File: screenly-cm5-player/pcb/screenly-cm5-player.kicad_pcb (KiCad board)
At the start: 2 copper layers, 120 x 90 mm, 1 part, among them U1 CM5104064

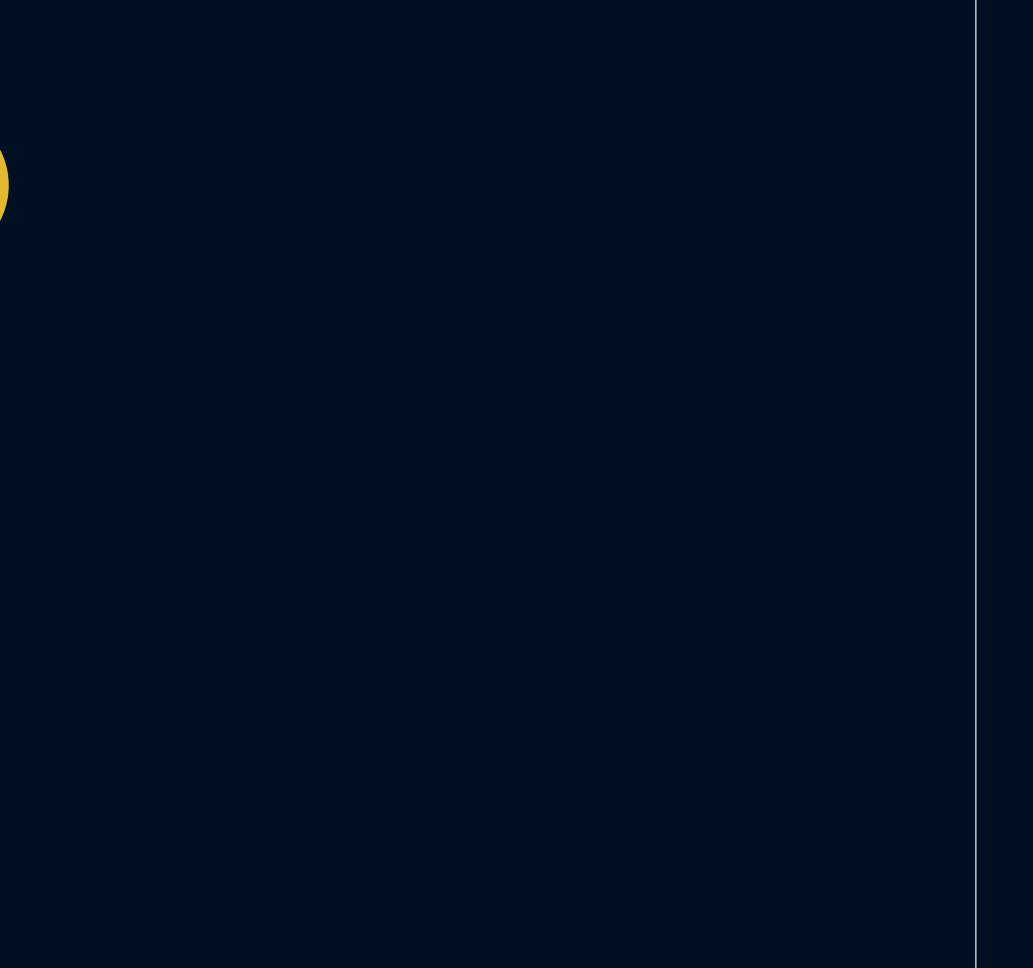
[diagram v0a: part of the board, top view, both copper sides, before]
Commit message: Power stage completed
All power stage has been completed. It has 3 different controlled
outputs USB and PCIe power are separated from the main power due to
safety, durability and cost reasons. PCIe will be DNP later.
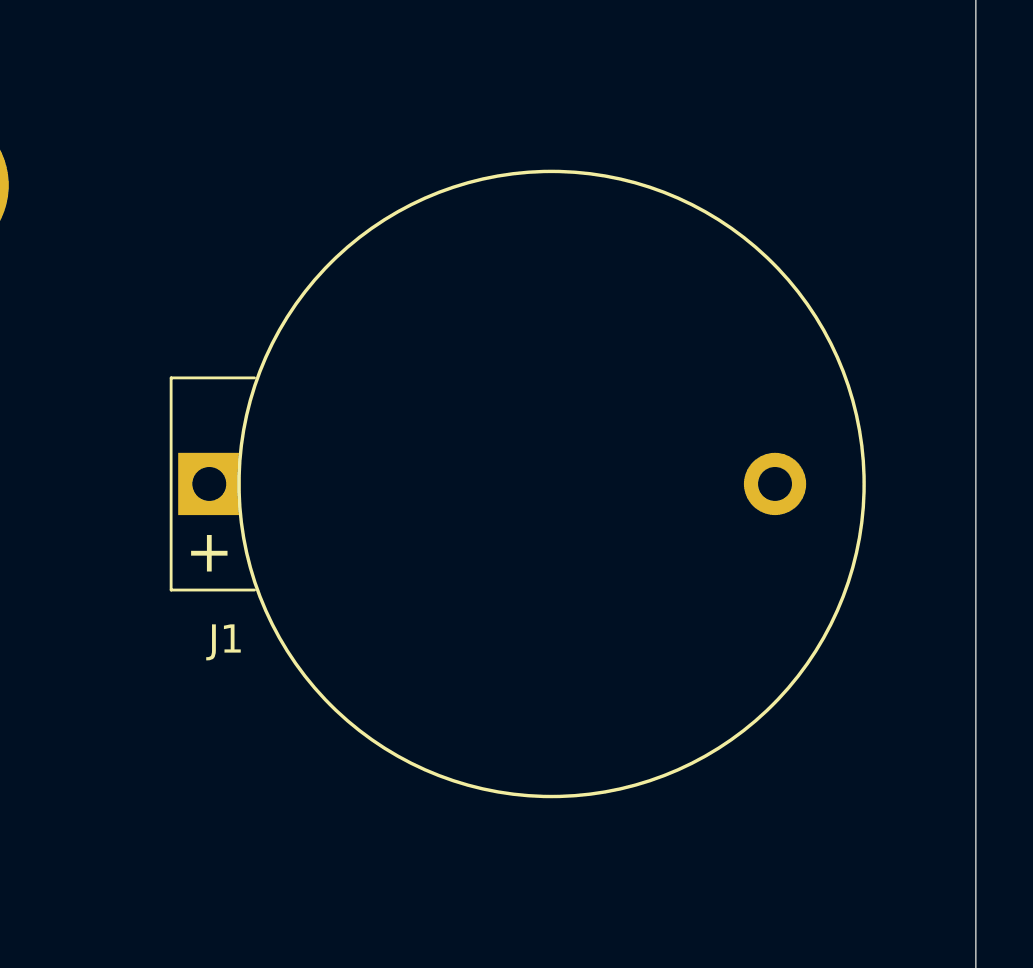
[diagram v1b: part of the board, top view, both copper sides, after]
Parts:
- added J1: CR2032 Holder, Screenly:BatteryHolder_MYOUNG_BS-02_CR2032, F.Cu at (190.0, 80.0)
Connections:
- U1 pad 1: unconnected-(U1A-GND-Pad1) -> GND
- U1 pad 10: unconnected-(U1A-Ethernet_Pair0_N-Pad10) -> /compute_module/ETH.TRD0_N
- U1 pad 100: unconnected-(U1A-CAM_GPIO1-Pad100) -> /compute_module/CAM_GPIO1
- U1 pad 101: unconnected-(U1B-USB_OTG_ID-Pad101) -> /compute_module/USBOTG_ID
- U1 pad 102: unconnected-(U1B-PCIe_nCLKREQ-Pad102) -> /compute_module/PCIE.nCLKREQ
- U1 pad 103: unconnected-(U1B-USB2_N-Pad103) -> /compute_module/USB2.D_N
- U1 pad 104: unconnected-(U1B-PCIE_nWAKE-Pad104) -> /compute_module/PCIE.nWAKE
- U1 pad 105: unconnected-(U1B-USB2_P-Pad105) -> /compute_module/USB2.D_P
- U1 pad 106: unconnected-(U1B-PCIE_PWR_EN-Pad106) -> /compute_module/PCIE.PWR_EN
- U1 pad 107: unconnected-(U1B-GND-Pad107) -> GND
- U1 pad 108: unconnected-(U1B-GND-Pad108) -> GND
- U1 pad 109: unconnected-(U1B-PCIe_nRST-Pad109) -> /compute_module/PCIE.nRST
- U1 pad 11: unconnected-(U1A-Ethernet_Pair2_P-Pad11) -> /compute_module/ETH.TRD2_P
- U1 pad 110: unconnected-(U1B-PCIe_CLK_P-Pad110) -> /compute_module/PCIE.CLK_P
- U1 pad 111: unconnected-(U1B-VBUS_EN-Pad111) -> /compute_module/VBUS_EN
- U1 pad 112: unconnected-(U1B-PCIe_CLK_N-Pad112) -> /compute_module/PCIE.CLK_N
- U1 pad 113: unconnected-(U1B-GND-Pad113) -> GND
- U1 pad 114: unconnected-(U1B-GND-Pad114) -> GND
- U1 pad 115: unconnected-(U1B-MIPI0_D0_N-Pad115) -> /compute_module/DPHY0_P.D0_N
- U1 pad 116: unconnected-(U1B-PCIe_RX_P-Pad116) -> /compute_module/PCIE.RX_P
- U1 pad 117: unconnected-(U1B-MIPI0_D0_P-Pad117) -> /compute_module/DPHY0_P.D0_P
- U1 pad 118: unconnected-(U1B-PCIe_RX_N-Pad118) -> /compute_module/PCIE.RX_N
- U1 pad 119: unconnected-(U1B-GND-Pad119) -> GND
- U1 pad 12: unconnected-(U1A-Ethernet_Pair0_P-Pad12) -> /compute_module/ETH.TRD0_P
- U1 pad 120: unconnected-(U1B-GND-Pad120) -> GND
- U1 pad 121: unconnected-(U1B-MIPI0_D1_N-Pad121) -> /compute_module/DPHY0_P.D1_N
- U1 pad 122: unconnected-(U1B-PCIe_TX_P-Pad122) -> /compute_module/PCIE.TX_P
- U1 pad 123: unconnected-(U1B-MIPI0_D1_P-Pad123) -> /compute_module/DPHY0_P.D1_P
- U1 pad 124: unconnected-(U1B-PCIe_TX_N-Pad124) -> /compute_module/PCIE.TX_N
- U1 pad 125: unconnected-(U1B-GND-Pad125) -> GND
- U1 pad 126: unconnected-(U1B-GND-Pad126) -> GND
- U1 pad 127: unconnected-(U1B-MIPI0_C_N-Pad127) -> /compute_module/DPHY0_P.C_N
- U1 pad 128: unconnected-(U1B-USB3-0-RX_N-Pad128) -> /compute_module/USB3_0.RX_N
- U1 pad 129: unconnected-(U1B-MIPI0_C_P-Pad129) -> /compute_module/DPHY0_P.C_P
- U1 pad 13: unconnected-(U1A-GND-Pad13) -> GND
- U1 pad 130: unconnected-(U1B-USB3-0-RX_P-Pad130) -> /compute_module/USB3_0.RX_P
- U1 pad 131: unconnected-(U1B-GND-Pad131) -> GND
- U1 pad 132: unconnected-(U1B-GND-Pad132) -> GND
- U1 pad 133: unconnected-(U1B-MIPI0_D2_N-Pad133) -> /compute_module/DPHY0_P.D2_N
- U1 pad 134: unconnected-(U1B-USB3-0-D_P-Pad134) -> /compute_module/USB3_0.D_P
- U1 pad 135: unconnected-(U1B-MIPI0_D2_P-Pad135) -> /compute_module/DPHY0_P.D2_P
- U1 pad 136: unconnected-(U1B-USB3-0-D_N-Pad136) -> /compute_module/USB3_0.D_N
- U1 pad 137: unconnected-(U1B-GND-Pad137) -> GND
- U1 pad 138: unconnected-(U1B-GND-Pad138) -> GND
- U1 pad 139: unconnected-(U1B-MIPI0_D3_N-Pad139) -> /compute_module/DPHY0_P.D3_N
- U1 pad 14: unconnected-(U1A-GND-Pad14) -> GND
- U1 pad 140: unconnected-(U1B-USB3-0-TX_N-Pad140) -> /compute_module/USB3_0.TX_N
- U1 pad 141: unconnected-(U1B-MIPI0_D3_P-Pad141) -> /compute_module/DPHY0_P.D3_P
- U1 pad 142: unconnected-(U1B-USB3-0-TX_P-Pad142) -> /compute_module/USB3_0.TX_P
- U1 pad 143: unconnected-(U1B-HDMI1_HOTPLUG-Pad143) -> /compute_module/HDMI1.HOTPLUG
- U1 pad 144: unconnected-(U1B-GND-Pad144) -> GND
- U1 pad 145: unconnected-(U1B-HDMI1_SDA-Pad145) -> /compute_module/HDMI1.SDA
- U1 pad 146: unconnected-(U1B-HDMI1_TX2_P-Pad146) -> /compute_module/HDMI1.D2_P
- U1 pad 147: unconnected-(U1B-HDMI1_SCL-Pad147) -> /compute_module/HDMI1.SCL
- U1 pad 148: unconnected-(U1B-HDMI1_TX2_N-Pad148) -> /compute_module/HDMI1.D2_N
- U1 pad 149: unconnected-(U1B-HDMI1_CEC-Pad149) -> /compute_module/HDMI1.CEC
- U1 pad 15: unconnected-(U1A-Ethernet_nLED3(3.3v)-Pad15) -> /compute_module/ETH_nLED_ACTIVITY
- U1 pad 150: unconnected-(U1B-GND-Pad150) -> GND
- U1 pad 151: unconnected-(U1B-HDMI0_CEC-Pad151) -> /compute_module/HDMI0.CEC
- U1 pad 152: unconnected-(U1B-HDMI1_TX1_P-Pad152) -> /compute_module/HDMI1.D1_P
- U1 pad 153: unconnected-(U1B-HDMI0_HOTPLUG-Pad153) -> /compute_module/HDMI0.HOTPLUG
- U1 pad 154: unconnected-(U1B-HDMI1_TX1_N-Pad154) -> /compute_module/HDMI1.D1_N
- U1 pad 155: unconnected-(U1B-GND-Pad155) -> GND
- U1 pad 156: unconnected-(U1B-GND-Pad156) -> GND
- U1 pad 157: unconnected-(U1B-USB3-1-RX_N-Pad157) -> /compute_module/USB3_1.RX_N
- U1 pad 158: unconnected-(U1B-HDMI1_TX0_P-Pad158) -> /compute_module/HDMI1.D0_P
- U1 pad 159: unconnected-(U1B-USB3-1-RX_P-Pad159) -> /compute_module/USB3_1.RX_P
- U1 pad 16: unconnected-(U1A-FAN_TACHO-Pad16) -> /compute_module/FAN_TACHO
- U1 pad 160: unconnected-(U1B-HDMI1_TX0_N-Pad160) -> /compute_module/HDMI1.D0_N
- U1 pad 161: unconnected-(U1B-GND-Pad161) -> GND
- U1 pad 162: unconnected-(U1B-GND-Pad162) -> GND
- U1 pad 163: unconnected-(U1B-USB3-1-D_P-Pad163) -> /compute_module/USB3_1.D_P
- U1 pad 164: unconnected-(U1B-HDMI1_CLK_P-Pad164) -> /compute_module/HDMI1.CK_P
- U1 pad 165: unconnected-(U1B-USB3-1-D_N-Pad165) -> /compute_module/USB3_1.D_N
- U1 pad 166: unconnected-(U1B-HDMI1_CLK_N-Pad166) -> /compute_module/HDMI1.CK_N
- U1 pad 167: unconnected-(U1B-GND-Pad167) -> GND
- U1 pad 168: unconnected-(U1B-GND-Pad168) -> GND
- U1 pad 169: unconnected-(U1B-USB3-1-TX_N-Pad169) -> /compute_module/USB3_1.TX_N
- U1 pad 17: unconnected-(U1A-Ethernet_nLED2(3.3v)-Pad17) -> /compute_module/nLED_SPEED_100_1000
- U1 pad 170: unconnected-(U1B-HDMI0_TX2_P-Pad170) -> /compute_module/HDMI0.D2_P
- U1 pad 171: unconnected-(U1B-USB3-1-TX_P-Pad171) -> /compute_module/USB3_1.TX_P
- U1 pad 172: unconnected-(U1B-HDMI0_TX2_N-Pad172) -> /compute_module/HDMI0.D2_N
- U1 pad 173: unconnected-(U1B-GND-Pad173) -> GND
- U1 pad 174: unconnected-(U1B-GND-Pad174) -> GND
- U1 pad 175: unconnected-(U1B-MIPI1_D0_N-Pad175) -> /compute_module/DPHY1_P.D0_N
- U1 pad 176: unconnected-(U1B-HDMI0_TX1_P-Pad176) -> /compute_module/HDMI0.D1_P
- U1 pad 177: unconnected-(U1B-MIPI1_D0_P-Pad177) -> /compute_module/DPHY1_P.D0_P
- U1 pad 178: unconnected-(U1B-HDMI0_TX1_N-Pad178) -> /compute_module/HDMI0.D1_N
- U1 pad 179: unconnected-(U1B-GND-Pad179) -> GND
- U1 pad 18: unconnected-(U1A-Ethernet_SYNC_OUT(3.3v)-Pad18) -> /compute_module/SYNC_OUT
- U1 pad 180: unconnected-(U1B-GND-Pad180) -> GND
- U1 pad 181: unconnected-(U1B-MIPI1_D1_N-Pad181) -> /compute_module/DPHY1_P.D1_N
- U1 pad 182: unconnected-(U1B-HDMI0_TX0_P-Pad182) -> /compute_module/HDMI0.D0_P
- U1 pad 183: unconnected-(U1B-MIPI1_D1_P-Pad183) -> /compute_module/DPHY1_P.D1_P
- U1 pad 184: unconnected-(U1B-HDMI0_TX0_N-Pad184) -> /compute_module/HDMI0.D0_N
- U1 pad 185: unconnected-(U1B-GND-Pad185) -> GND
- U1 pad 186: unconnected-(U1B-GND-Pad186) -> GND
- U1 pad 187: unconnected-(U1B-MIPI1_C_N-Pad187) -> /compute_module/DPHY1_P.C_N
- U1 pad 188: unconnected-(U1B-HDMI0_CLK_P-Pad188) -> /compute_module/HDMI0.CK_P
- U1 pad 189: unconnected-(U1B-MIPI1_C_P-Pad189) -> /compute_module/DPHY1_P.C_P
- U1 pad 19: unconnected-(U1A-FAN_PWM-Pad19) -> /compute_module/FAN_PWM
- U1 pad 190: unconnected-(U1B-HDMI0_CLK_N-Pad190) -> /compute_module/HDMI0.CK_N
- U1 pad 191: unconnected-(U1B-GND-Pad191) -> GND
- U1 pad 192: unconnected-(U1B-GND-Pad192) -> GND
- U1 pad 193: unconnected-(U1B-MIPI1_D2_N-Pad193) -> /compute_module/DPHY1_P.D2_N
- U1 pad 194: unconnected-(U1B-MIPI1_D3_N-Pad194) -> /compute_module/DPHY1_P.D3_N
- U1 pad 195: unconnected-(U1B-MIPI1_D2_P-Pad195) -> /compute_module/DPHY1_P.D2_P
- U1 pad 196: unconnected-(U1B-MIPI1_D3_P-Pad196) -> /compute_module/DPHY1_P.D3_P
- U1 pad 197: unconnected-(U1B-GND-Pad197) -> GND
- U1 pad 198: unconnected-(U1B-GND-Pad198) -> GND
- U1 pad 199: unconnected-(U1B-HDMI0_SDA-Pad199) -> /compute_module/HDMI0.SDA
- U1 pad 2: unconnected-(U1A-GND-Pad2) -> GND
- U1 pad 20: unconnected-(U1A-EEPROM_nWP-Pad20) -> /compute_module/EEPROM_nWP
- U1 pad 200: unconnected-(U1B-HDMI0_SCL-Pad200) -> /compute_module/HDMI0.SCL
- U1 pad 21: unconnected-(U1A-LED_nACT-Pad21) -> /compute_module/nLED_ACTIVITY
- U1 pad 22: unconnected-(U1A-GND-Pad22) -> GND
- U1 pad 23: unconnected-(U1A-GND-Pad23) -> GND
- U1 pad 24: unconnected-(U1A-GPIO26-Pad24) -> /compute_module/GPIO26
- U1 pad 25: unconnected-(U1A-GPIO21-Pad25) -> /compute_module/SCLK_GPIO21
- U1 pad 26: unconnected-(U1A-GPIO19-Pad26) -> /compute_module/MISO_GPIO19
- U1 pad 27: unconnected-(U1A-GPIO20-Pad27) -> /compute_module/MOSI_GPIO20
- U1 pad 28: unconnected-(U1A-GPIO13-Pad28) -> /compute_module/GPIO13
- U1 pad 29: unconnected-(U1A-GPIO16-Pad29) -> /compute_module/GPIO16
- U1 pad 3: unconnected-(U1A-Ethernet_Pair3_P-Pad3) -> /compute_module/ETH.TRD3_P
- U1 pad 30: unconnected-(U1A-GPIO6-Pad30) -> /compute_module/GPIO6
- U1 pad 31: unconnected-(U1A-GPIO12-Pad31) -> /compute_module/GPIO12
- U1 pad 32: unconnected-(U1A-GND-Pad32) -> GND
- U1 pad 33: unconnected-(U1A-GND-Pad33) -> GND
- U1 pad 34: unconnected-(U1A-GPIO5-Pad34) -> /compute_module/GPIO5
- U1 pad 35: unconnected-(U1A-ID_SC-Pad35) -> /compute_module/ID_SC
- U1 pad 36: unconnected-(U1A-ID_SD-Pad36) -> /compute_module/ID_SD
- U1 pad 37: unconnected-(U1A-GPIO7-Pad37) -> /compute_module/GPIO7
- U1 pad 38: unconnected-(U1A-GPIO11-Pad38) -> /compute_module/GPIO11
- U1 pad 39: unconnected-(U1A-GPIO8-Pad39) -> /compute_module/GPIO8
- U1 pad 4: unconnected-(U1A-Ethernet_Pair1_P-Pad4) -> /compute_module/ETH.TRD1_P
- U1 pad 40: unconnected-(U1A-GPIO9-Pad40) -> /compute_module/GPIO9
- U1 pad 41: unconnected-(U1A-GPIO25-Pad41) -> /compute_module/DC_GPI25
- U1 pad 42: unconnected-(U1A-GND-Pad42) -> GND
- U1 pad 43: unconnected-(U1A-GND-Pad43) -> GND
- U1 pad 44: unconnected-(U1A-GPIO10-Pad44) -> /compute_module/GPIO10
- U1 pad 45: unconnected-(U1A-GPIO24-Pad45) -> /compute_module/BL_GPIO24
- U1 pad 46: unconnected-(U1A-GPIO22-Pad46) -> /compute_module/GPIO22
- U1 pad 47: unconnected-(U1A-GPIO23-Pad47) -> /compute_module/GPIO23
- U1 pad 48: unconnected-(U1A-GPIO27-Pad48) -> /compute_module/RST_GPIO27
- U1 pad 49: unconnected-(U1A-GPIO18-Pad49) -> /compute_module/CS_GPIO18
- U1 pad 5: unconnected-(U1A-Ethernet_Pair3_N-Pad5) -> /compute_module/ETH.TRD3_N
- U1 pad 50: unconnected-(U1A-GPIO17-Pad50) -> /compute_module/GPIO17
- U1 pad 51: unconnected-(U1A-GPIO15-Pad51) -> /compute_module/GPIO15
- U1 pad 52: unconnected-(U1A-GND-Pad52) -> GND
- U1 pad 53: unconnected-(U1A-GND-Pad53) -> GND
- U1 pad 54: unconnected-(U1A-GPIO4-Pad54) -> /compute_module/GPIO4
- U1 pad 55: unconnected-(U1A-GPIO14-Pad55) -> /compute_module/GPIO14
- U1 pad 56: unconnected-(U1A-GPIO3-Pad56) -> /compute_module/SCL1_IO3
- U1 pad 57: unconnected-(U1A-SD_CLK-Pad57) -> /compute_module/SD_CLK
- U1 pad 58: unconnected-(U1A-GPIO2-Pad58) -> /compute_module/SDA1_IO2
- U1 pad 59: unconnected-(U1A-GND-Pad59) -> GND
- U1 pad 6: unconnected-(U1A-Ethernet_Pair1_N-Pad6) -> /compute_module/ETH.TRD1_N
- U1 pad 60: unconnected-(U1A-GND-Pad60) -> GND
- U1 pad 61: unconnected-(U1A-SD_DAT3-Pad61) -> /compute_module/SD_DAT3
- U1 pad 62: unconnected-(U1A-SD_CMD-Pad62) -> /compute_module/SD_CMD
- U1 pad 63: unconnected-(U1A-SD_DAT0-Pad63) -> /compute_module/SD_DAT0
- U1 pad 65: unconnected-(U1A-GND-Pad65) -> GND
- U1 pad 66: unconnected-(U1A-GND-Pad66) -> GND
- U1 pad 67: unconnected-(U1A-SD_DAT1-Pad67) -> /compute_module/SD_DAT1
- U1 pad 69: unconnected-(U1A-SD_DAT2-Pad69) -> /compute_module/SD_DAT2
- U1 pad 7: unconnected-(U1A-GND-Pad7) -> GND
- U1 pad 71: unconnected-(U1A-GND-Pad71) -> GND
- U1 pad 74: unconnected-(U1A-GND-Pad74) -> GND
- U1 pad 75: unconnected-(U1A-SD_PWR_ON-Pad75) -> /compute_module/SD_PWR_ON
- U1 pad 76: unconnected-(U1A-VBAT-Pad76) -> +BATT
- U1 pad 77: unconnected-(U1A-+5v_(Input)-Pad77) -> /compute_module/+5V
- U1 pad 78: unconnected-(U1A-GPIO_VREF(1.8v/3.3v_Input)-Pad78) -> /compute_module/GPIO_VREF
- U1 pad 79: unconnected-(U1A-+5v_(Input)-Pad79) -> /compute_module/+5V
- U1 pad 8: unconnected-(U1A-GND-Pad8) -> GND
- U1 pad 80: unconnected-(U1A-SCL0-Pad80) -> /compute_module/SCL0
- U1 pad 81: unconnected-(U1A-+5v_(Input)-Pad81) -> /compute_module/+5V
- U1 pad 82: unconnected-(U1A-SDA0-Pad82) -> /compute_module/SDA0
- U1 pad 83: unconnected-(U1A-+5v_(Input)-Pad83) -> /compute_module/+5V
- U1 pad 84: unconnected-(U1A-+3.3v_(Output)-Pad84) -> /compute_module/3V3_CM4
- U1 pad 85: unconnected-(U1A-+5v_(Input)-Pad85) -> /compute_module/+5V
- U1 pad 86: unconnected-(U1A-+3.3v_(Output)-Pad86) -> /compute_module/3V3_CM4
- U1 pad 87: unconnected-(U1A-+5v_(Input)-Pad87) -> /compute_module/+5V
- U1 pad 88: unconnected-(U1A-+1.8v_(Output)-Pad88) -> /compute_module/1V8_CM4
- U1 pad 89: unconnected-(U1A-WiFi_nDisable-Pad89) -> /compute_module/WL_nDis
- U1 pad 9: unconnected-(U1A-Ethernet_Pair2_N-Pad9) -> /compute_module/ETH.TRD2_N
- U1 pad 90: unconnected-(U1A-+1.8v_(Output)-Pad90) -> /compute_module/1V8_CM4
- U1 pad 91: unconnected-(U1A-BT_nDisable-Pad91) -> /compute_module/BT_nDis
- U1 pad 92: unconnected-(U1A-PWR_BUT-Pad92) -> /compute_module/PWR_BUT
- U1 pad 93: unconnected-(U1A-nRPIBOOT-Pad93) -> /compute_module/nRPIBOOT
- U1 pad 94: unconnected-(U1A-CC1-Pad94) -> /compute_module/CC1
- U1 pad 95: unconnected-(U1A-LED_nPWR-Pad95) -> /compute_module/PI_nLED_PWR
- U1 pad 96: unconnected-(U1A-CC2-Pad96) -> /compute_module/CC2
- U1 pad 97: unconnected-(U1A-CAM_GPIO0-Pad97) -> /compute_module/CAM_GPIO0
- U1 pad 98: unconnected-(U1A-GND-Pad98) -> GND
- U1 pad 99: unconnected-(U1A-PMIC_ENABLE-Pad99) -> /compute_module/GLOBAL_EN

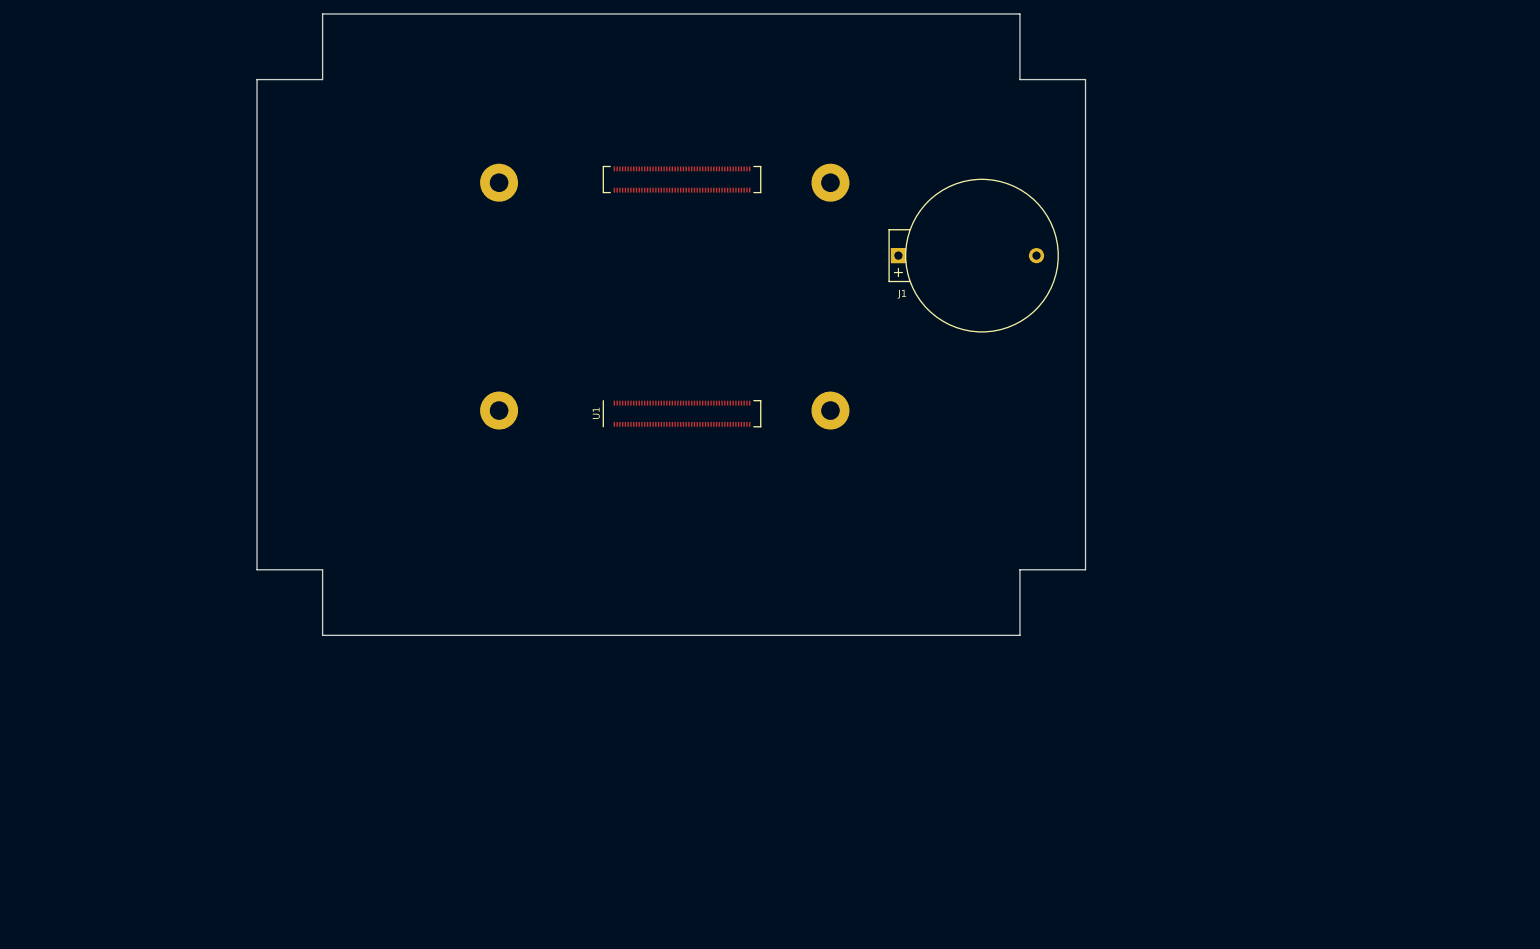
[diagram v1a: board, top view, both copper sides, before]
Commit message: Ethernet and PCIe sections are done.
Modified power section and moved PCIe specific circuit into its own
section.
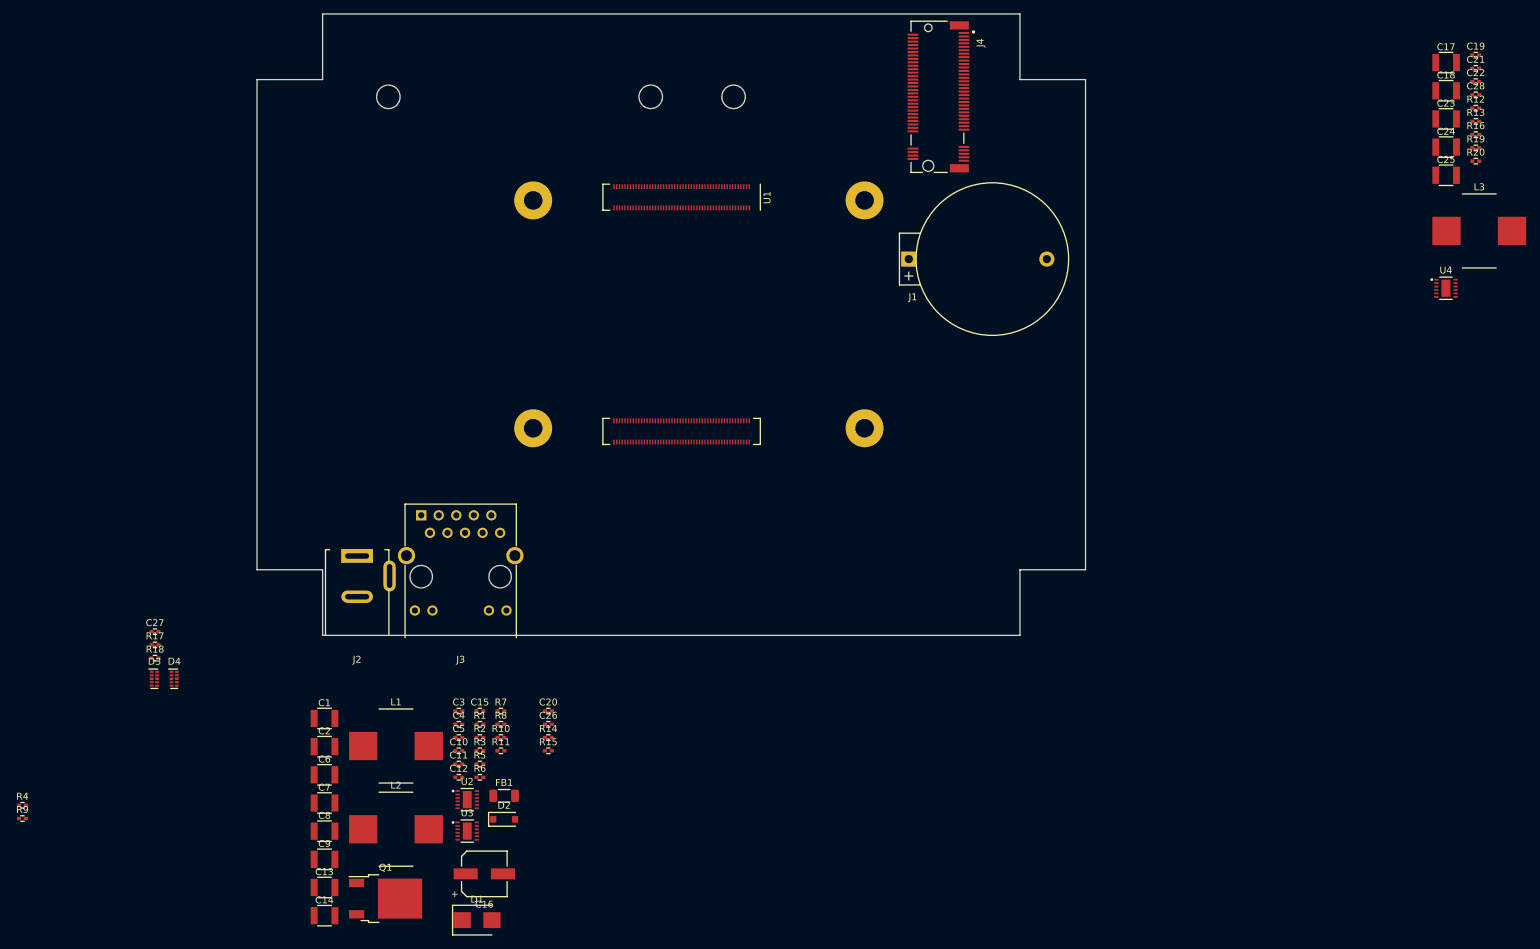
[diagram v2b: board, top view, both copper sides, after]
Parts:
- added C1: 10uF, Screenly:C_1210, F.Cu at (94.8, 147.0)
- added C10: 100nF, Screenly:C_0402, F.Cu at (114.2, 151.7)
- added C11: 100nF, Screenly:C_0402, F.Cu at (114.2, 153.6)
- added C12: 33pF, Screenly:C_0402, F.Cu at (114.2, 155.6)
- added C13: 47uF, Screenly:C_1210, F.Cu at (94.8, 171.5)
- added C14: 47uF, Screenly:C_1210, F.Cu at (94.8, 175.6)
- added C15: 100nF, Screenly:C_0402, F.Cu at (117.3, 146.0)
- added C16: 100uF, Screenly:CP_Elec_6.3x7.7, F.Cu at (117.9, 169.5)
- added C17: 10uF, Screenly:C_1210, F.Cu at (257.2, 52.0)
- added C18: 10uF, Screenly:C_1210, F.Cu at (257.2, 56.1)
- added C19: 100nF, Screenly:C_0402, F.Cu at (261.5, 51.0)
- added C2: 10uF, Screenly:C_1210, F.Cu at (94.8, 151.1)
- added C20: 100nF, Screenly:C_0402, F.Cu at (127.2, 146.0)
- added C21: 100nF, Screenly:C_0402, F.Cu at (261.5, 52.9)
- added C22: 33pF, Screenly:C_0402, F.Cu at (261.5, 54.8)
- added C23: 47uF, Screenly:C_1210, F.Cu at (257.2, 60.2)
- added C24: 47uF, Screenly:C_1210, F.Cu at (257.2, 64.3)
- added C25: 47uF, Screenly:C_1210, F.Cu at (257.2, 68.4)
- added C26: 100nF, Screenly:C_0402, F.Cu at (127.2, 147.9)
- added C27: 100nF, Screenly:C_0402, F.Cu at (70.2, 134.5)
- added C28: 100nF, Screenly:C_0402, F.Cu at (261.5, 56.7)
- added C3: 100nF, Screenly:C_0402, F.Cu at (114.2, 146.0)
- added C4: 100nF, Screenly:C_0402, F.Cu at (114.2, 147.9)
- added C5: 33pF, Screenly:C_0402, F.Cu at (114.2, 149.8)
- added C6: 47uF, Screenly:C_1210, F.Cu at (94.8, 155.2)
- added C7: 47uF, Screenly:C_1210, F.Cu at (94.8, 159.3)
- added C8: 10uF, Screenly:C_1210, F.Cu at (94.8, 163.4)
- added C9: 10uF, Screenly:C_1210, F.Cu at (94.8, 167.4)
- added D1: SMBJ18CA, Screenly:D_SMB, F.Cu at (116.9, 176.2)
- added D2: 12V, Screenly:D_SOD-123, F.Cu at (120.8, 161.6)
- added D3: TPD4EUSB30DQAR, Screenly:TI_USON-10_2.5x1.0mm_P0.5mm, F.Cu at (70.1, 141.3)
- added D4: TPD4EUSB30DQAR, Screenly:TI_USON-10_2.5x1.0mm_P0.5mm, F.Cu at (73.0, 141.3)
- added FB1: 50R, Screenly:FB_1206, F.Cu at (120.8, 158.2)
- added J2: DC Jack 5.5x2.1mm, Screenly:BarrelJack_Tensility_54-00129_Horizontal, F.Cu at (99.5, 126.4)
- added J3: HB-W01G0520DQW-R, Screenly:RJ45_Hanbo_HB-W01G0520DQW-R_Horizontal, F.Cu at (114.5, 126.5)
- added J4: SM3ZS067U410AMR1000, Screenly:M2_M-Key_JAE_SM3ZS067U410AMR1000_2230_2242_2280, F.Cu at (182.2, 57.0)
- added L1: 4.7uH, Screenly:L_Coilank_AAPS1050, F.Cu at (105.1, 151.0)
- added L2: 4.7uH, Screenly:L_Coilank_AAPS1050, F.Cu at (105.1, 163.1)
- added L3: 4.7uH, Screenly:L_Coilank_AAPS1050, F.Cu at (262.0, 76.4)
- added Q1: AOD4185, Screenly:TO-252-2, F.Cu at (103.6, 173.1)
- added R1: 100K, Screenly:R_0402, F.Cu at (117.3, 147.9)
- added R10: 1K, Screenly:R_0402, F.Cu at (120.3, 149.8)
- added R11: 100K, Screenly:R_0402, F.Cu at (120.3, 151.7)
- added R12: 100K, Screenly:R_0402, F.Cu at (261.5, 58.6)
- added R13: 31.6K, Screenly:R_0402, F.Cu at (261.5, 60.6)
- added R14: 100K, Screenly:R_0402, F.Cu at (127.2, 149.8)
- added R15: 100K, Screenly:R_0402, F.Cu at (127.2, 151.7)
- added R16: 1K, Screenly:R_0402, F.Cu at (261.5, 62.5)
- added R17: 470, Screenly:R_0402, F.Cu at (70.2, 136.4)
- added R18: 470, Screenly:R_0402, F.Cu at (70.2, 138.3)
- added R19: 100K, Screenly:R_0402, F.Cu at (261.5, 64.4)
- added R2: 470K, Screenly:R_0402, F.Cu at (117.3, 149.8)
- added R20: 120, Screenly:R_0402, F.Cu at (261.5, 66.3)
- added R3: 100K, Screenly:R_0402, F.Cu at (117.3, 151.7)
- added R4: 19.1K, Screenly:R_0402, F.Cu at (51.0, 159.6)
- added R5: 1K, Screenly:R_0402, F.Cu at (117.3, 153.6)
- added R6: 120, Screenly:R_0402, F.Cu at (117.3, 155.6)
- added R7: 100K, Screenly:R_0402, F.Cu at (120.3, 146.0)
- added R8: 100K, Screenly:R_0402, F.Cu at (120.3, 147.9)
- added R9: 19.1K, Screenly:R_0402, F.Cu at (51.0, 161.5)
- added U2: LMR51450SDRRR, Screenly:TI_WSON-12-1EP_3x3mm_P0.5mm_EP1.3x2.5mm, F.Cu at (115.5, 158.8)
- added U3: LMR51450SDRRR, Screenly:TI_WSON-12-1EP_3x3mm_P0.5mm_EP1.3x2.5mm, F.Cu at (115.5, 163.3)
- added U4: LMR51450SDRRR, Screenly:TI_WSON-12-1EP_3x3mm_P0.5mm_EP1.3x2.5mm, F.Cu at (257.2, 84.7)
- moved U1 52.7 mm to (125.0, 72.0), turned to -90 degrees
- moved J1 1.58 mm to (191.5, 80.5)
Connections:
- net /compute_module/+5V renamed +5V
- net /compute_module/1V8_CM4 renamed +1V8
- net /compute_module/3V3_CM4 renamed +3V3
- net /compute_module/BL_GPIO24 renamed /Compute Module/BL_GPIO24
- net /compute_module/CAM_GPIO1 renamed /Compute Module/CAM_GPIO1
- net /compute_module/CC1 renamed /Compute Module/CC1
- net /compute_module/CC2 renamed /Compute Module/CC2
- net /compute_module/CS_GPIO18 renamed /Compute Module/CS_GPIO18
- net /compute_module/DC_GPI25 renamed /Compute Module/DC_GPI25
- net /compute_module/DPHY0_P.C_N renamed /Compute Module/DPHY0_P.C_N
- net /compute_module/DPHY0_P.C_P renamed /Compute Module/DPHY0_P.C_P
- net /compute_module/DPHY0_P.D0_N renamed /Compute Module/DPHY0_P.D0_N
- net /compute_module/DPHY0_P.D0_P renamed /Compute Module/DPHY0_P.D0_P
- net /compute_module/DPHY0_P.D1_N renamed /Compute Module/DPHY0_P.D1_N
- net /compute_module/DPHY0_P.D1_P renamed /Compute Module/DPHY0_P.D1_P
- net /compute_module/DPHY0_P.D2_N renamed /Compute Module/DPHY0_P.D2_N
- net /compute_module/DPHY0_P.D2_P renamed /Compute Module/DPHY0_P.D2_P
- net /compute_module/DPHY0_P.D3_N renamed /Compute Module/DPHY0_P.D3_N
- net /compute_module/DPHY0_P.D3_P renamed /Compute Module/DPHY0_P.D3_P
- net /compute_module/DPHY1_P.C_N renamed /Compute Module/DPHY1_P.C_N
- net /compute_module/DPHY1_P.C_P renamed /Compute Module/DPHY1_P.C_P
- net /compute_module/DPHY1_P.D0_N renamed /Compute Module/DPHY1_P.D0_N
- net /compute_module/DPHY1_P.D0_P renamed /Compute Module/DPHY1_P.D0_P
- net /compute_module/DPHY1_P.D1_N renamed /Compute Module/DPHY1_P.D1_N
- net /compute_module/DPHY1_P.D1_P renamed /Compute Module/DPHY1_P.D1_P
- net /compute_module/DPHY1_P.D2_N renamed /Compute Module/DPHY1_P.D2_N
- net /compute_module/DPHY1_P.D2_P renamed /Compute Module/DPHY1_P.D2_P
- net /compute_module/DPHY1_P.D3_N renamed /Compute Module/DPHY1_P.D3_N
- net /compute_module/DPHY1_P.D3_P renamed /Compute Module/DPHY1_P.D3_P
- net /compute_module/EEPROM_nWP renamed /Compute Module/~{EEPROM_WP}
- net /compute_module/ETH_nLED_ACTIVITY renamed /Compute Module/~{ETH_LED_ACT}
- net /compute_module/GLOBAL_EN renamed /Compute Module/GLOBAL_EN
- net /compute_module/GPIO_VREF renamed /Compute Module/GPIO_VREF
- net /compute_module/HDMI0.CEC renamed /Compute Module/HDMI0.CEC
- net /compute_module/HDMI0.CK_N renamed /Compute Module/HDMI0.CK_N
- net /compute_module/HDMI0.CK_P renamed /Compute Module/HDMI0.CK_P
- net /compute_module/HDMI0.D0_N renamed /Compute Module/HDMI0.D0_N
- net /compute_module/HDMI0.D0_P renamed /Compute Module/HDMI0.D0_P
- net /compute_module/HDMI0.D1_N renamed /Compute Module/HDMI0.D1_N
- net /compute_module/HDMI0.D1_P renamed /Compute Module/HDMI0.D1_P
- net /compute_module/HDMI0.D2_N renamed /Compute Module/HDMI0.D2_N
- net /compute_module/HDMI0.D2_P renamed /Compute Module/HDMI0.D2_P
- net /compute_module/HDMI0.HOTPLUG renamed /Compute Module/HDMI0.HOTPLUG
- net /compute_module/HDMI0.SCL renamed /Compute Module/HDMI0.SCL
- net /compute_module/HDMI0.SDA renamed /Compute Module/HDMI0.SDA
- net /compute_module/HDMI1.CEC renamed /Compute Module/HDMI1.CEC
- net /compute_module/HDMI1.CK_N renamed /Compute Module/HDMI1.CK_N
- net /compute_module/HDMI1.CK_P renamed /Compute Module/HDMI1.CK_P
- net /compute_module/HDMI1.D0_N renamed /Compute Module/HDMI1.D0_N
- net /compute_module/HDMI1.D0_P renamed /Compute Module/HDMI1.D0_P
- net /compute_module/HDMI1.D1_N renamed /Compute Module/HDMI1.D1_N
- net /compute_module/HDMI1.D1_P renamed /Compute Module/HDMI1.D1_P
- net /compute_module/HDMI1.D2_N renamed /Compute Module/HDMI1.D2_N
- net /compute_module/HDMI1.D2_P renamed /Compute Module/HDMI1.D2_P
- net /compute_module/HDMI1.HOTPLUG renamed /Compute Module/HDMI1.HOTPLUG
- net /compute_module/HDMI1.SCL renamed /Compute Module/HDMI1.SCL
- net /compute_module/HDMI1.SDA renamed /Compute Module/HDMI1.SDA
- net /compute_module/ID_SC renamed /Compute Module/ID_SC
- net /compute_module/ID_SD renamed /Compute Module/ID_SD
- net /compute_module/MISO_GPIO19 renamed /Compute Module/MISO_GPIO19
- net /compute_module/MOSI_GPIO20 renamed /Compute Module/MOSI_GPIO20
- net /compute_module/PWR_BUT renamed /Compute Module/PWR_BTN
- net /compute_module/RST_GPIO27 renamed /Compute Module/RST_GPIO27
- net /compute_module/SCLK_GPIO21 renamed /Compute Module/SCLK_GPIO21
- net /compute_module/SD_CLK renamed /Compute Module/SD_CARD.CLK
- net /compute_module/SD_CMD renamed /Compute Module/SD_CARD.CMD
- net /compute_module/SD_DAT0 renamed /Compute Module/SD_CARD.D0
- net /compute_module/SD_DAT1 renamed /Compute Module/SD_CARD.D1
- net /compute_module/SD_DAT2 renamed /Compute Module/SD_CARD.D2
- net /compute_module/SD_DAT3 renamed /Compute Module/SD_CARD.D3
- net /compute_module/SD_PWR_ON renamed /Compute Module/SD_CARD.PWR_ON
- net /compute_module/USB2.D_N renamed /Compute Module/USB2.D_N
- net /compute_module/USB2.D_P renamed /Compute Module/USB2.D_P
- net /compute_module/USB3_0.D_N renamed /Compute Module/USB3_0.D_N
- net /compute_module/USB3_0.D_P renamed /Compute Module/USB3_0.D_P
- net /compute_module/USB3_0.RX_N renamed /Compute Module/USB3_0.RX_N
- net /compute_module/USB3_0.RX_P renamed /Compute Module/USB3_0.RX_P
- net /compute_module/USB3_0.TX_N renamed /Compute Module/USB3_0.TX_N
- net /compute_module/USB3_0.TX_P renamed /Compute Module/USB3_0.TX_P
- net /compute_module/USB3_1.D_N renamed /Compute Module/USB3_1.D_N
- net /compute_module/USB3_1.D_P renamed /Compute Module/USB3_1.D_P
- net /compute_module/USB3_1.RX_N renamed /Compute Module/USB3_1.RX_N
- net /compute_module/USB3_1.RX_P renamed /Compute Module/USB3_1.RX_P
- net /compute_module/USB3_1.TX_N renamed /Compute Module/USB3_1.TX_N
- net /compute_module/USB3_1.TX_P renamed /Compute Module/USB3_1.TX_P
- net /compute_module/USBOTG_ID renamed /Compute Module/USBOTG_ID
- net /compute_module/VBUS_EN renamed /Compute Module/VBUS_EN
- net /compute_module/nLED_SPEED_100_1000 renamed /Compute Module/~{ETH_LED_SPD}
- net /compute_module/nRPIBOOT renamed /Compute Module/~{RPIBOOT}
- U1 pad 10: /compute_module/ETH.TRD0_N -> /Compute Module/ETH.TRD0_N
- U1 pad 102: /compute_module/PCIE.nCLKREQ -> /Compute Module/PCIE.nCLKREQ
- U1 pad 104: /compute_module/PCIE.nWAKE -> /Compute Module/PCIE.nWAKE
- U1 pad 106: /compute_module/PCIE.PWR_EN -> /Compute Module/PCIE.PWR_EN
- U1 pad 109: /compute_module/PCIE.nRST -> /Compute Module/PCIE.nRST
- U1 pad 11: /compute_module/ETH.TRD2_P -> /Compute Module/ETH.TRD2_P
- U1 pad 110: /compute_module/PCIE.CLK_P -> /Compute Module/PCIE.CLK_P
- U1 pad 112: /compute_module/PCIE.CLK_N -> /Compute Module/PCIE.CLK_N
- U1 pad 116: /compute_module/PCIE.RX_P -> /Compute Module/PCIE.RX_P
- U1 pad 118: /compute_module/PCIE.RX_N -> /Compute Module/PCIE.RX_N
- U1 pad 12: /compute_module/ETH.TRD0_P -> /Compute Module/ETH.TRD0_P
- U1 pad 122: /compute_module/PCIE.TX_P -> /Compute Module/PCIE.TX_P
- U1 pad 124: /compute_module/PCIE.TX_N -> /Compute Module/PCIE.TX_N
- U1 pad 16: /compute_module/FAN_TACHO -> unconnected-(U1A-FAN_TACHO-Pad16)
- U1 pad 18: /compute_module/SYNC_OUT -> unconnected-(U1A-Ethernet_SYNC_OUT(3.3v)-Pad18)
- U1 pad 19: /compute_module/FAN_PWM -> unconnected-(U1A-FAN_PWM-Pad19)
- U1 pad 21: /compute_module/nLED_ACTIVITY -> /Compute Module/~{CM5_LED_ACT}
- U1 pad 24: /compute_module/GPIO26 -> unconnected-(U1A-GPIO26-Pad24)
- U1 pad 28: /compute_module/GPIO13 -> unconnected-(U1A-GPIO13-Pad28)
- U1 pad 29: /compute_module/GPIO16 -> unconnected-(U1A-GPIO16-Pad29)
- U1 pad 3: /compute_module/ETH.TRD3_P -> /Compute Module/ETH.TRD3_P
- U1 pad 30: /compute_module/GPIO6 -> unconnected-(U1A-GPIO6-Pad30)
- U1 pad 31: /compute_module/GPIO12 -> unconnected-(U1A-GPIO12-Pad31)
- U1 pad 34: /compute_module/GPIO5 -> unconnected-(U1A-GPIO5-Pad34)
- U1 pad 37: /compute_module/GPIO7 -> unconnected-(U1A-GPIO7-Pad37)
- U1 pad 38: /compute_module/GPIO11 -> unconnected-(U1A-GPIO11-Pad38)
- U1 pad 39: /compute_module/GPIO8 -> unconnected-(U1A-GPIO8-Pad39)
- U1 pad 4: /compute_module/ETH.TRD1_P -> /Compute Module/ETH.TRD1_P
- U1 pad 40: /compute_module/GPIO9 -> unconnected-(U1A-GPIO9-Pad40)
- U1 pad 44: /compute_module/GPIO10 -> unconnected-(U1A-GPIO10-Pad44)
- U1 pad 46: /compute_module/GPIO22 -> unconnected-(U1A-GPIO22-Pad46)
- U1 pad 47: /compute_module/GPIO23 -> unconnected-(U1A-GPIO23-Pad47)
- U1 pad 5: /compute_module/ETH.TRD3_N -> /Compute Module/ETH.TRD3_N
- U1 pad 50: /compute_module/GPIO17 -> unconnected-(U1A-GPIO17-Pad50)
- U1 pad 51: /compute_module/GPIO15 -> unconnected-(U1A-GPIO15-Pad51)
- U1 pad 54: /compute_module/GPIO4 -> unconnected-(U1A-GPIO4-Pad54)
- U1 pad 55: /compute_module/GPIO14 -> unconnected-(U1A-GPIO14-Pad55)
- U1 pad 56: /compute_module/SCL1_IO3 -> unconnected-(U1A-GPIO3-Pad56)
- U1 pad 58: /compute_module/SDA1_IO2 -> unconnected-(U1A-GPIO2-Pad58)
- U1 pad 6: /compute_module/ETH.TRD1_N -> /Compute Module/ETH.TRD1_N
- U1 pad 64: unconnected-(U1A-SD_DAT5-Pad64) -> /Compute Module/SD_CARD.D5
- U1 pad 68: unconnected-(U1A-SD_DAT4-Pad68) -> /Compute Module/SD_CARD.D4
- U1 pad 70: unconnected-(U1A-SD_DAT7-Pad70) -> /Compute Module/SD_CARD.D7
- U1 pad 72: unconnected-(U1A-SD_DAT6-Pad72) -> /Compute Module/SD_CARD.D6
- U1 pad 80: /compute_module/SCL0 -> unconnected-(U1A-SCL0-Pad80)
- U1 pad 82: /compute_module/SDA0 -> unconnected-(U1A-SDA0-Pad82)
- U1 pad 89: /compute_module/WL_nDis -> unconnected-(U1A-WiFi_nDisable-Pad89)
- U1 pad 9: /compute_module/ETH.TRD2_N -> /Compute Module/ETH.TRD2_N
- U1 pad 91: /compute_module/BT_nDis -> unconnected-(U1A-BT_nDisable-Pad91)
- U1 pad 95: /compute_module/PI_nLED_PWR -> /Compute Module/~{CM5_LED_PWR}
- U1 pad 97: /compute_module/CAM_GPIO0 -> unconnected-(U1A-CAM_GPIO0-Pad97)
